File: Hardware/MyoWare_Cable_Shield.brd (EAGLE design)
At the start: 52.3 x 20.8 mm, 13 parts

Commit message: Revert "V11"
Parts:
- added LOGO: (no value), advancer-technologies:MYOWARE_LOGO
- added SPIRAL: (no value), advancer-technologies:SPIRAL_LOGO_60%
- added U$6: (no value), advancer-technologies:ADVANCER_LOGO
- moved JP1 28.2 mm to (-22.0, 2.54)
- moved LOGO2 28.2 mm to (12.7, 0.00)
- moved STANDOFF2 28.2 mm to (22.2, -6.48)
- moved FID1 28.2 mm to (17.0, -8.00)
- moved FID2 28.2 mm to (-17.0, 8.00)
- moved FRAME1 28.2 mm to (-31.8, -25.4)
- moved JP2 28.2 mm to (-24.6, 2.54)
- moved JP3 28.2 mm to (0.00, 10.4)
- moved JP5 28.2 mm to (24.6, 2.54)
- moved JP6 28.2 mm to (22.0, 2.54)
- moved LOGO1 28.2 mm to (-12.7, -2.54)
- moved STANDOFF1 28.2 mm to (-22.2, 6.48)
- moved JP4 27.5 mm to (8.38, -8.89)
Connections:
- net END: now also JP3.TIP; no longer JP3.RING
- net MID: now also JP3.SLEEVE; no longer JP3.TIP
- net VREF: now also JP3.RING; no longer JP3.SLEEVE
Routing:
- net END: track 26.7 -> 11.7 mm, vias 1 -> 0
- net MID: track 12.4 -> 22.5 mm
- net VREF: track 20.0 -> 26.7 mm, vias 1 -> 0
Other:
- board text added: "Revised by: Brent Wilkins"
- board text added: "v10"
- board text removed: "Revised by: Elizabeth Robert"
- board text removed: "v11"

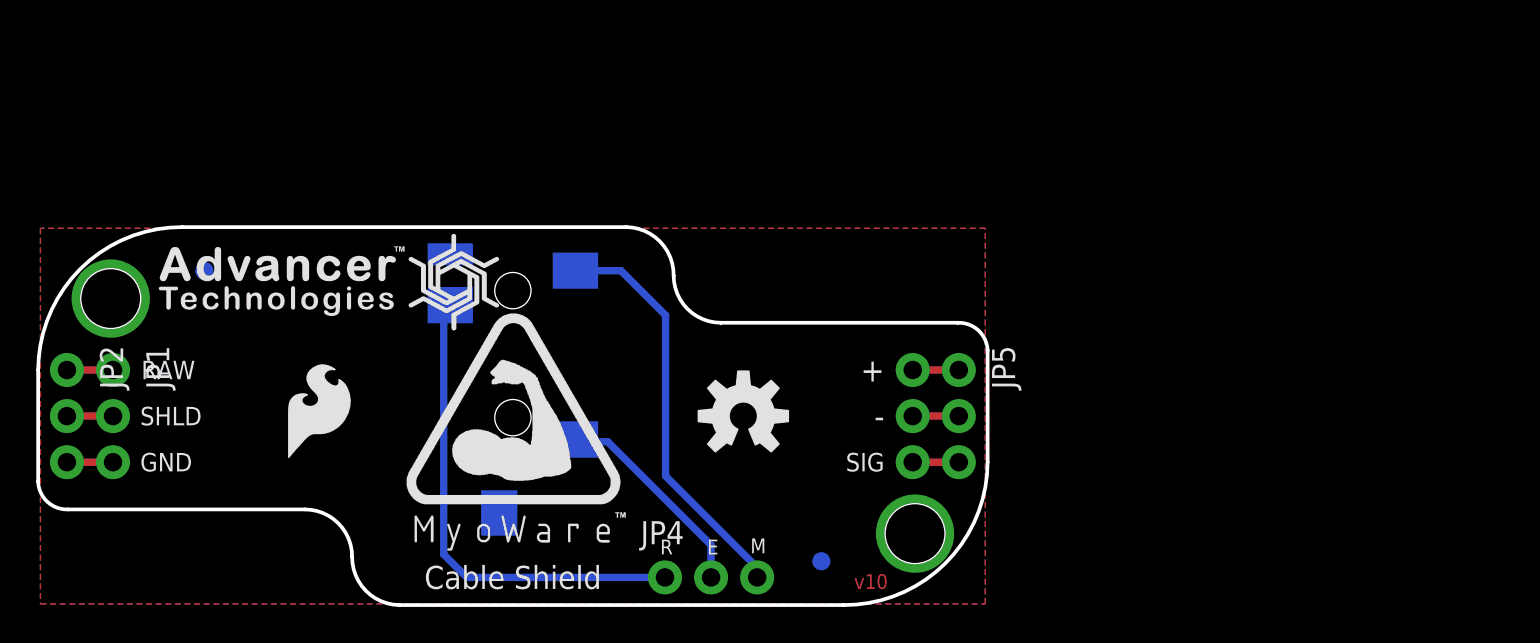
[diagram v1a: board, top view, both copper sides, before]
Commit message: V11
REM Headers Lining Up
Traces Adjusted
Board Origin Fix
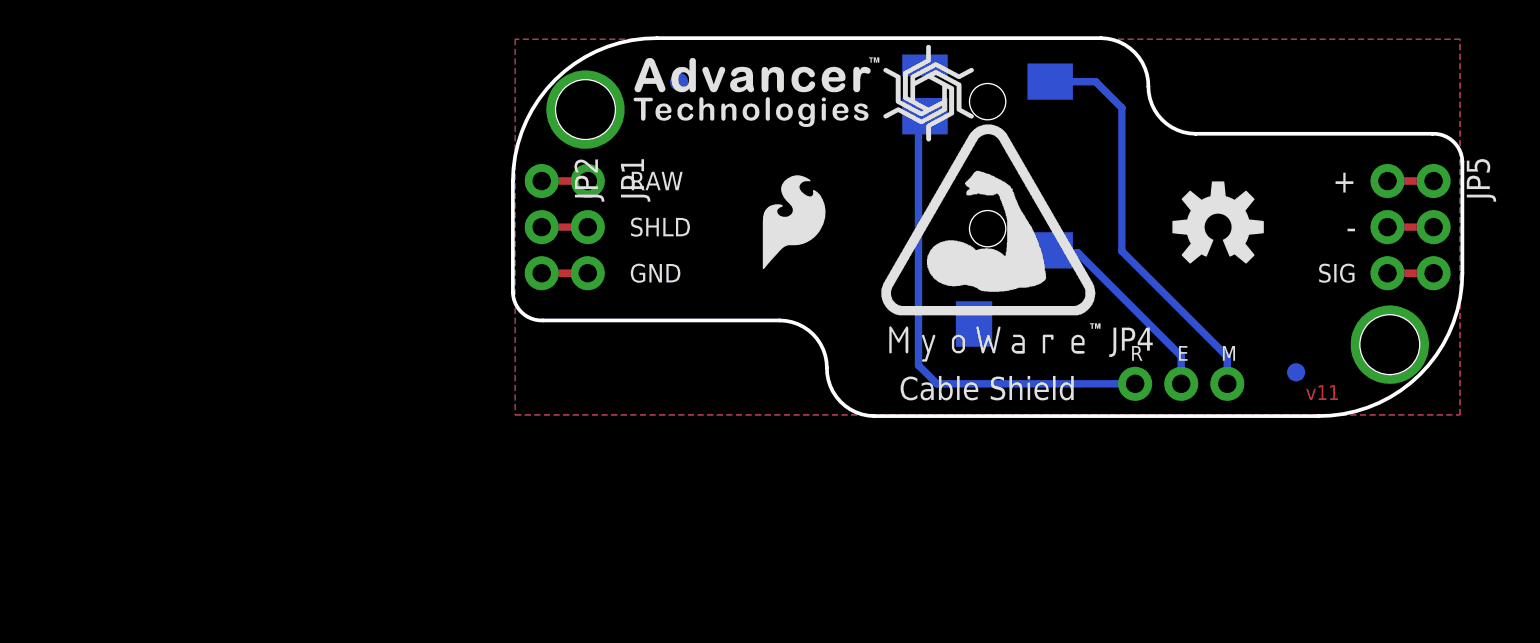
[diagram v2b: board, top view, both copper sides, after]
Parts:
- moved JP1 28.2 mm to (4.13, 13.0)
- moved LOGO2 28.2 mm to (38.9, 10.4)
- moved STANDOFF2 28.2 mm to (48.3, 3.94)
- moved FID1 28.2 mm to (43.2, 2.41)
- moved FID2 28.2 mm to (9.16, 18.4)
- moved FRAME1 28.2 mm to (-5.59, -15.0)
- moved JP2 28.2 mm to (1.59, 13.0)
- moved JP3 28.2 mm to (26.2, 20.8)
- moved JP5 28.2 mm to (50.7, 13.0)
- moved JP6 28.2 mm to (48.2, 13.0)
- moved LOGO 28.2 mm to (26.2, 9.53)
- moved LOGO1 28.2 mm to (13.5, 7.87)
- moved SPIRAL 28.2 mm to (22.9, 17.8)
- moved STANDOFF1 28.2 mm to (4.00, 16.9)
- moved U$6 28.2 mm to (13.1, 17.6)
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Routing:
- net END: track 11.7 -> 11.2 mm
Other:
- board text added: "Revised by: Elizabeth Robert"
- board text added: "v11"
- board text removed: "Revised by: Brent Wilkins"
- board text removed: "v10"

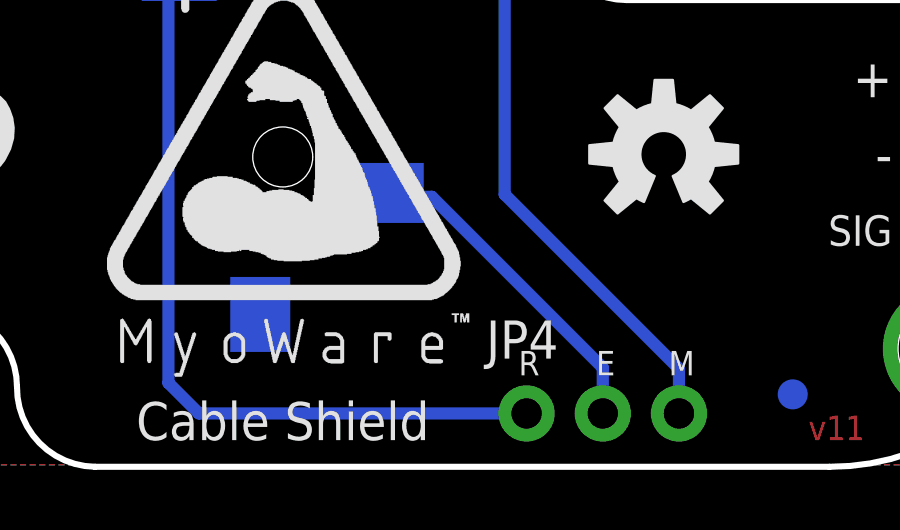
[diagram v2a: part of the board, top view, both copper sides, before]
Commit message: V11 Small Change to REM Position
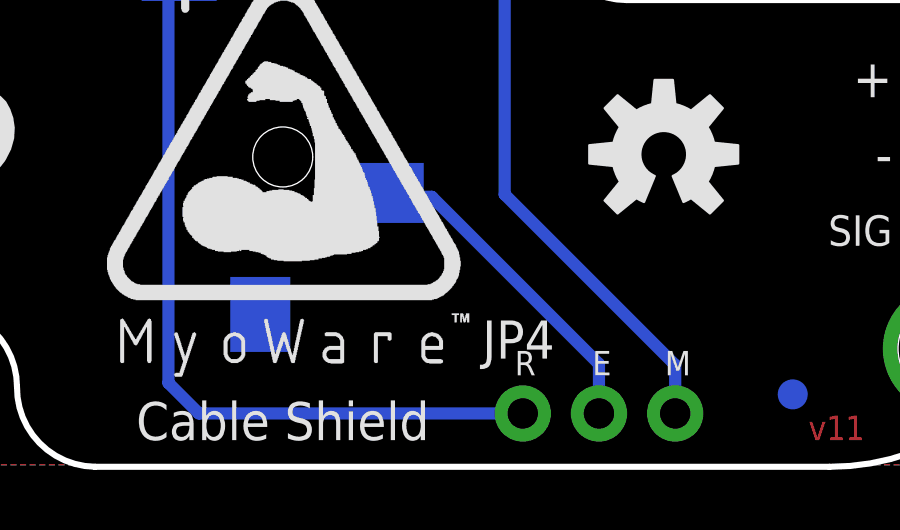
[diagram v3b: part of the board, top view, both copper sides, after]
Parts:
- moved JP4 0.13 mm to (34.2, 1.78)
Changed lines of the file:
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@@
 <wire x1="19.90725" y1="0" x2="44.3865" y2="0" width="0.2032" layer="20"/>
 <wire x1="32.41675" y1="20.828" x2="7.9375" y2="20.828" width="0.2032" layer="20"/>
-<text x="39.4589" y="3.048" size="0.8128" layer="21" font="vector" ratio="20" align="bottom-center">M</text>
-<text x="34.37255" y="3.048" size="0.8128" layer="21" font="vector" ratio="20" align="bottom-center">R</text>
-<text x="36.92525" y="3.048" size="0.8128" layer="21" font="vector" ratio="20" align="bottom-center">E</text>
+<text x="39.3319" y="3.048" size="0.8128" layer="21" font="vector" ratio="20" align="bottom-center">M</text>
+<text x="34.24555" y="3.048" size="0.8128" layer="21" font="vector" ratio="20" align="bottom-center">R</text>
+<text x="36.79825" y="3.048" size="0.8128" layer="21" font="vector" ratio="20" align="bottom-center">E</text>
 <text x="6.4262" y="12.954" size="1.016" layer="21" font="vector" ratio="17" align="center-left">RAW</text>
 <text x="6.4262" y="10.414" size="1.016" layer="21" font="vector" ratio="17" align="center-left">SHLD</text>
@@
 <text x="6.2738" y="10.414" size="1.016" layer="22" font="vector" ratio="17" rot="MR0" align="center-right">SHLD</text>
 <text x="6.2738" y="7.874" size="1.016" layer="22" font="vector" ratio="17" rot="MR0" align="center-right">GND</text>
-<text x="39.30141875" y="3.048" size="0.8128" layer="22" font="vector" ratio="20" rot="MR0" align="bottom-center">M</text>
-<text x="34.20745" y="3.048" size="0.8128" layer="22" font="vector" ratio="20" rot="MR0" align="bottom-center">R</text>
-<text x="36.76015" y="3.048" size="0.8128" layer="22" font="vector" ratio="20" rot="MR0" align="bottom-center">E</text>
+<text x="39.17315" y="3.048" size="0.8128" layer="22" font="vector" ratio="20" rot="MR0" align="bottom-center">M</text>
+<text x="34.09315" y="3.048" size="0.8128" layer="22" font="vector" ratio="20" rot="MR0" align="bottom-center">R</text>
+<text x="36.63315" y="3.048" size="0.8128" layer="22" font="vector" ratio="20" rot="MR0" align="bottom-center">E</text>
 <wire x1="50.673" y1="15.5575" x2="52.324" y2="14.0335" width="0.2032" layer="20" curve="-90"/>
 <dimension x1="-6.25475" y1="-10.414" x2="-18.2245" y2="10.414" x3="-34.29" y3="0" textsize="1.778" textratio="15" layer="47" dtype="vertical" unit="inch"/>
@@
 <element name="LOGO" library="advancer-technologies" package="MYOWARE_LOGO" value="" x="26.162" y="9.525"/>
 <element name="SPIRAL" library="advancer-technologies" package="SPIRAL_LOGO_60%" value="" x="22.9489" y="17.7927"/>
-<element name="JP4" library="SparkFun-Connectors" package="1X03_NO_SILK" value="Power" x="34.29" y="1.778"/>
+<element name="JP4" library="SparkFun-Connectors" package="1X03_NO_SILK" value="Power" x="34.163" y="1.778"/>
 <element name="JP5" library="SparkFun-Connectors" package="1X03_NO_SILK" value="Power" x="50.7365" y="12.954" rot="R270"/>
 <element name="JP2" library="SparkFun-Connectors" package="1X03_NO_SILK" value="Power" x="1.5875" y="12.954" rot="R270"/>
@@
 <contactref element="JP4" pad="3"/>
 <wire x1="33.55975" y1="16.98625" x2="33.55975" y2="9.077959375" width="0.4064" layer="16"/>
-<wire x1="33.55975" y1="9.077959375" x2="39.37" y2="3.267709375" width="0.4064" layer="16"/>
+<wire x1="33.55975" y1="9.077959375" x2="39.243" y2="3.394709375" width="0.4064" layer="16"/>
 <contactref element="JP3" pad="SLEEVE"/>
 <wire x1="29.612" y1="18.428" x2="32.118" y2="18.428" width="0.4064" layer="16"/>
 <wire x1="32.118" y1="18.428" x2="33.55975" y2="16.98625" width="0.4064" layer="16"/>
-<wire x1="39.37" y1="1.778" x2="39.37" y2="3.267709375" width="0.4064" layer="16"/>
+<wire x1="39.243" y1="1.778" x2="39.243" y2="3.394709375" width="0.4064" layer="16"/>
 </signal>
 <signal name="END">
 <contactref element="JP4" pad="2"/>
-<wire x1="36.83" y1="3.302" x2="31.133034375" y2="8.999" width="0.4064" layer="16"/>
+<wire x1="36.703" y1="3.429" x2="31.133034375" y2="8.999" width="0.4064" layer="16"/>
 <contactref element="JP3" pad="TIP"/>
 <wire x1="31.133034375" y1="8.999" x2="29.61513125" y2="8.999" width="0.4064" layer="16"/>
 <wire x1="29.61513125" y1="8.999" x2="29.612" y2="9.128" width="0.4064" layer="16"/>
-<wire x1="36.83" y1="1.778" x2="36.83" y2="3.302" width="0.4064" layer="16"/>
+<wire x1="36.703" y1="1.778" x2="36.703" y2="3.429" width="0.4064" layer="16"/>
 </signal>
 <signal name="VREF">
 <contactref element="JP4" pad="1"/>
-<wire x1="34.29" y1="1.778" x2="23.368" y2="1.778" width="0.4064" layer="16"/>
+<wire x1="34.163" y1="1.778" x2="23.368" y2="1.778" width="0.4064" layer="16"/>
 <wire x1="23.368" y1="1.778" x2="22.352" y2="2.794" width="0.4064" layer="16"/>
 <wire x1="22.352" y1="2.794" x2="22.352" y2="16.389" width="0.4064" layer="16"/>

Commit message: Minor Adjustment
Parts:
- moved JP4 0.14 mm to (34.1, 1.65)
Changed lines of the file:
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@@
 <?xml version="1.0" encoding="utf-8"?>
 <!DOCTYPE eagle SYSTEM "eagle.dtd">
-<eagle version="7.2.0">
+<eagle version="7.7.0">
 <drawing>
 <settings>
@@
 <wire x1="19.90725" y1="0" x2="44.3865" y2="0" width="0.2032" layer="20"/>
 <wire x1="32.41675" y1="20.828" x2="7.9375" y2="20.828" width="0.2032" layer="20"/>
-<text x="39.3319" y="3.048" size="0.8128" layer="21" font="vector" ratio="20" align="bottom-center">M</text>
-<text x="34.24555" y="3.048" size="0.8128" layer="21" font="vector" ratio="20" align="bottom-center">R</text>
-<text x="36.79825" y="3.048" size="0.8128" layer="21" font="vector" ratio="20" align="bottom-center">E</text>
+<text x="39.2811" y="3.048" size="0.8128" layer="21" font="vector" ratio="20" align="bottom-center">M</text>
+<text x="34.19475" y="3.048" size="0.8128" layer="21" font="vector" ratio="20" align="bottom-center">R</text>
+<text x="36.74745" y="3.048" size="0.8128" layer="21" font="vector" ratio="20" align="bottom-center">E</text>
 <text x="6.4262" y="12.954" size="1.016" layer="21" font="vector" ratio="17" align="center-left">RAW</text>
 <text x="6.4262" y="10.414" size="1.016" layer="21" font="vector" ratio="17" align="center-left">SHLD</text>
@@
 <text x="6.2738" y="10.414" size="1.016" layer="22" font="vector" ratio="17" rot="MR0" align="center-right">SHLD</text>
 <text x="6.2738" y="7.874" size="1.016" layer="22" font="vector" ratio="17" rot="MR0" align="center-right">GND</text>
-<text x="39.17315" y="3.048" size="0.8128" layer="22" font="vector" ratio="20" rot="MR0" align="bottom-center">M</text>
-<text x="34.09315" y="3.048" size="0.8128" layer="22" font="vector" ratio="20" rot="MR0" align="bottom-center">R</text>
-<text x="36.63315" y="3.048" size="0.8128" layer="22" font="vector" ratio="20" rot="MR0" align="bottom-center">E</text>
+<text x="39.12235" y="3.048" size="0.8128" layer="22" font="vector" ratio="20" rot="MR0" align="bottom-center">M</text>
+<text x="34.04235" y="3.048" size="0.8128" layer="22" font="vector" ratio="20" rot="MR0" align="bottom-center">R</text>
+<text x="36.58235" y="3.048" size="0.8128" layer="22" font="vector" ratio="20" rot="MR0" align="bottom-center">E</text>
 <wire x1="50.673" y1="15.5575" x2="52.324" y2="14.0335" width="0.2032" layer="20" curve="-90"/>
 <dimension x1="-6.25475" y1="-10.414" x2="-18.2245" y2="10.414" x3="-34.29" y3="0" textsize="1.778" textratio="15" layer="47" dtype="vertical" unit="inch"/>
@@
 <element name="LOGO" library="advancer-technologies" package="MYOWARE_LOGO" value="" x="26.162" y="9.525"/>
 <element name="SPIRAL" library="advancer-technologies" package="SPIRAL_LOGO_60%" value="" x="22.9489" y="17.7927"/>
-<element name="JP4" library="SparkFun-Connectors" package="1X03_NO_SILK" value="Power" x="34.163" y="1.778"/>
+<element name="JP4" library="SparkFun-Connectors" package="1X03_NO_SILK" value="Power" x="34.1122" y="1.651"/>
 <element name="JP5" library="SparkFun-Connectors" package="1X03_NO_SILK" value="Power" x="50.7365" y="12.954" rot="R270"/>
 <element name="JP2" library="SparkFun-Connectors" package="1X03_NO_SILK" value="Power" x="1.5875" y="12.954" rot="R270"/>
@@
 <contactref element="JP4" pad="3"/>
 <wire x1="33.55975" y1="16.98625" x2="33.55975" y2="9.077959375" width="0.4064" layer="16"/>
-<wire x1="33.55975" y1="9.077959375" x2="39.243" y2="3.394709375" width="0.4064" layer="16"/>
+<wire x1="33.55975" y1="9.077959375" x2="39.1922" y2="3.445509375" width="0.4064" layer="16"/>
 <contactref element="JP3" pad="SLEEVE"/>
 <wire x1="29.612" y1="18.428" x2="32.118" y2="18.428" width="0.4064" layer="16"/>
 <wire x1="32.118" y1="18.428" x2="33.55975" y2="16.98625" width="0.4064" layer="16"/>
-<wire x1="39.243" y1="1.778" x2="39.243" y2="3.394709375" width="0.4064" layer="16"/>
+<wire x1="39.1922" y1="1.651" x2="39.1922" y2="3.445509375" width="0.4064" layer="16"/>
 </signal>
 <signal name="END">
 <contactref element="JP4" pad="2"/>
-<wire x1="36.703" y1="3.429" x2="31.133034375" y2="8.999" width="0.4064" layer="16"/>
+<wire x1="36.6522" y1="3.4798" x2="31.133034375" y2="8.999" width="0.4064" layer="16"/>
 <contactref element="JP3" pad="TIP"/>
 <wire x1="31.133034375" y1="8.999" x2="29.61513125" y2="8.999" width="0.4064" layer="16"/>
 <wire x1="29.61513125" y1="8.999" x2="29.612" y2="9.128" width="0.4064" layer="16"/>
-<wire x1="36.703" y1="1.778" x2="36.703" y2="3.429" width="0.4064" layer="16"/>
+<wire x1="36.6522" y1="1.651" x2="36.6522" y2="3.4798" width="0.4064" layer="16"/>
 </signal>
 <signal name="VREF">
 <contactref element="JP4" pad="1"/>
-<wire x1="34.163" y1="1.778" x2="23.368" y2="1.778" width="0.4064" layer="16"/>
-<wire x1="23.368" y1="1.778" x2="22.352" y2="2.794" width="0.4064" layer="16"/>
+<wire x1="34.1122" y1="1.651" x2="23.495" y2="1.651" width="0.4064" layer="16"/>
+<wire x1="23.495" y1="1.651" x2="22.352" y2="2.794" width="0.4064" layer="16"/>
 <wire x1="22.352" y1="2.794" x2="22.352" y2="16.389" width="0.4064" layer="16"/>
 <contactref element="JP3" pad="RING"/>

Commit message: Final Adjust before Protos
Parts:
- moved JP4 0.30 mm to (33.8, 1.65)
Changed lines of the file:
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@@
 <?xml version="1.0" encoding="utf-8"?>
 <!DOCTYPE eagle SYSTEM "eagle.dtd">
-<eagle version="7.7.0">
+<eagle version="7.2.0">
 <drawing>
 <settings>
@@
 <wire x1="19.90725" y1="0" x2="44.3865" y2="0" width="0.2032" layer="20"/>
 <wire x1="32.41675" y1="20.828" x2="7.9375" y2="20.828" width="0.2032" layer="20"/>
-<text x="39.2811" y="3.048" size="0.8128" layer="21" font="vector" ratio="20" align="bottom-center">M</text>
-<text x="34.19475" y="3.048" size="0.8128" layer="21" font="vector" ratio="20" align="bottom-center">R</text>
-<text x="36.74745" y="3.048" size="0.8128" layer="21" font="vector" ratio="20" align="bottom-center">E</text>
+<text x="38.9763" y="3.175" size="0.8128" layer="21" font="vector" ratio="20" align="bottom-center">M</text>
+<text x="33.88995" y="3.175" size="0.8128" layer="21" font="vector" ratio="20" align="bottom-center">R</text>
+<text x="36.44265" y="3.175" size="0.8128" layer="21" font="vector" ratio="20" align="bottom-center">E</text>
 <text x="6.4262" y="12.954" size="1.016" layer="21" font="vector" ratio="17" align="center-left">RAW</text>
 <text x="6.4262" y="10.414" size="1.016" layer="21" font="vector" ratio="17" align="center-left">SHLD</text>
@@
 <text x="6.2738" y="10.414" size="1.016" layer="22" font="vector" ratio="17" rot="MR0" align="center-right">SHLD</text>
 <text x="6.2738" y="7.874" size="1.016" layer="22" font="vector" ratio="17" rot="MR0" align="center-right">GND</text>
-<text x="39.12235" y="3.048" size="0.8128" layer="22" font="vector" ratio="20" rot="MR0" align="bottom-center">M</text>
-<text x="34.04235" y="3.048" size="0.8128" layer="22" font="vector" ratio="20" rot="MR0" align="bottom-center">R</text>
-<text x="36.58235" y="3.048" size="0.8128" layer="22" font="vector" ratio="20" rot="MR0" align="bottom-center">E</text>
+<text x="38.81755" y="3.175" size="0.8128" layer="22" font="vector" ratio="20" rot="MR0" align="bottom-center">M</text>
+<text x="33.73755" y="3.175" size="0.8128" layer="22" font="vector" ratio="20" rot="MR0" align="bottom-center">R</text>
+<text x="36.27755" y="3.175" size="0.8128" layer="22" font="vector" ratio="20" rot="MR0" align="bottom-center">E</text>
 <wire x1="50.673" y1="15.5575" x2="52.324" y2="14.0335" width="0.2032" layer="20" curve="-90"/>
 <dimension x1="-6.25475" y1="-10.414" x2="-18.2245" y2="10.414" x3="-34.29" y3="0" textsize="1.778" textratio="15" layer="47" dtype="vertical" unit="inch"/>
@@
 <element name="LOGO" library="advancer-technologies" package="MYOWARE_LOGO" value="" x="26.162" y="9.525"/>
 <element name="SPIRAL" library="advancer-technologies" package="SPIRAL_LOGO_60%" value="" x="22.9489" y="17.7927"/>
-<element name="JP4" library="SparkFun-Connectors" package="1X03_NO_SILK" value="Power" x="34.1122" y="1.651"/>
+<element name="JP4" library="SparkFun-Connectors" package="1X03_NO_SILK" value="Power" x="33.8074" y="1.651"/>
 <element name="JP5" library="SparkFun-Connectors" package="1X03_NO_SILK" value="Power" x="50.7365" y="12.954" rot="R270"/>
 <element name="JP2" library="SparkFun-Connectors" package="1X03_NO_SILK" value="Power" x="1.5875" y="12.954" rot="R270"/>
@@
 <contactref element="JP4" pad="3"/>
 <wire x1="33.55975" y1="16.98625" x2="33.55975" y2="9.077959375" width="0.4064" layer="16"/>
-<wire x1="33.55975" y1="9.077959375" x2="39.1922" y2="3.445509375" width="0.4064" layer="16"/>
+<wire x1="33.55975" y1="9.077959375" x2="38.8874" y2="3.750309375" width="0.4064" layer="16"/>
 <contactref element="JP3" pad="SLEEVE"/>
 <wire x1="29.612" y1="18.428" x2="32.118" y2="18.428" width="0.4064" layer="16"/>
 <wire x1="32.118" y1="18.428" x2="33.55975" y2="16.98625" width="0.4064" layer="16"/>
-<wire x1="39.1922" y1="1.651" x2="39.1922" y2="3.445509375" width="0.4064" layer="16"/>
+<wire x1="38.8874" y1="1.651" x2="38.8874" y2="3.750309375" width="0.4064" layer="16"/>
 </signal>
 <signal name="END">
 <contactref element="JP4" pad="2"/>
-<wire x1="36.6522" y1="3.4798" x2="31.133034375" y2="8.999" width="0.4064" layer="16"/>
+<wire x1="36.3474" y1="3.7846" x2="31.133034375" y2="8.999" width="0.4064" layer="16"/>
 <contactref element="JP3" pad="TIP"/>
 <wire x1="31.133034375" y1="8.999" x2="29.61513125" y2="8.999" width="0.4064" layer="16"/>
 <wire x1="29.61513125" y1="8.999" x2="29.612" y2="9.128" width="0.4064" layer="16"/>
-<wire x1="36.6522" y1="1.651" x2="36.6522" y2="3.4798" width="0.4064" layer="16"/>
+<wire x1="36.3474" y1="1.651" x2="36.3474" y2="3.7846" width="0.4064" layer="16"/>
 </signal>
 <signal name="VREF">
 <contactref element="JP4" pad="1"/>
-<wire x1="34.1122" y1="1.651" x2="23.495" y2="1.651" width="0.4064" layer="16"/>
+<wire x1="33.8074" y1="1.651" x2="23.495" y2="1.651" width="0.4064" layer="16"/>
 <wire x1="23.495" y1="1.651" x2="22.352" y2="2.794" width="0.4064" layer="16"/>
 <wire x1="22.352" y1="2.794" x2="22.352" y2="16.389" width="0.4064" layer="16"/>

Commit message: Replaced bitmap logos with vector logos
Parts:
- removed LOGO: (no value), advancer-technologies:MYOWARE_LOGO
- removed SPIRAL: (no value), advancer-technologies:SPIRAL_LOGO_60%
- removed U$6: (no value), advancer-technologies:ADVANCER_LOGO
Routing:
- net N$3: track 0.00 -> 664.4 mm
